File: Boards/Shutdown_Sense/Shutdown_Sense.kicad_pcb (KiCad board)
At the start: 2 copper layers, 76.2 x 67.3 mm, 68 parts, among them IC1 ATMEGA16M1, J2 MM_F_RA_20, J3 CONN_02X03, Q3 SSM3K333R, Q4 SSM3K333R, U101 TPS560430YF, U3 CAN_Transceiver, Y1 Crystal_SMD

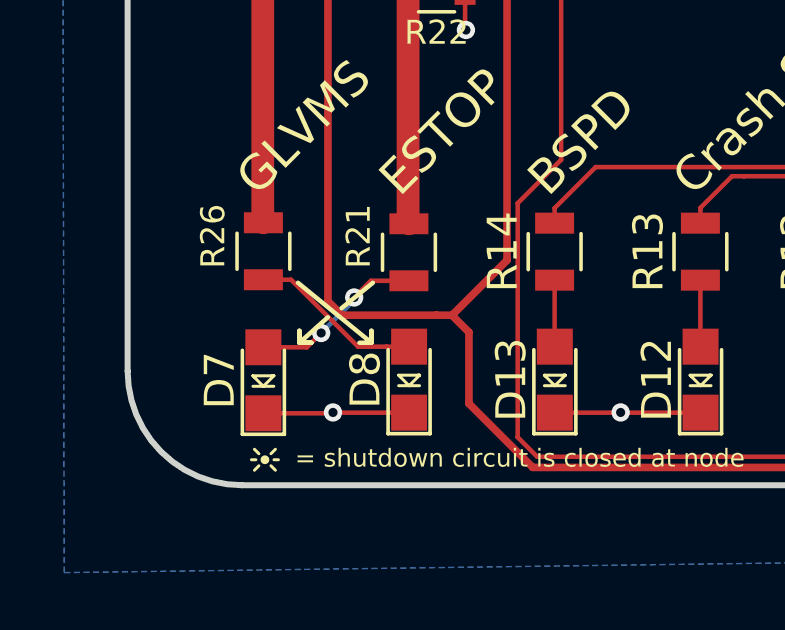
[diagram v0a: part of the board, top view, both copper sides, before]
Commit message: Fix SR-latch language in BSPD schematic
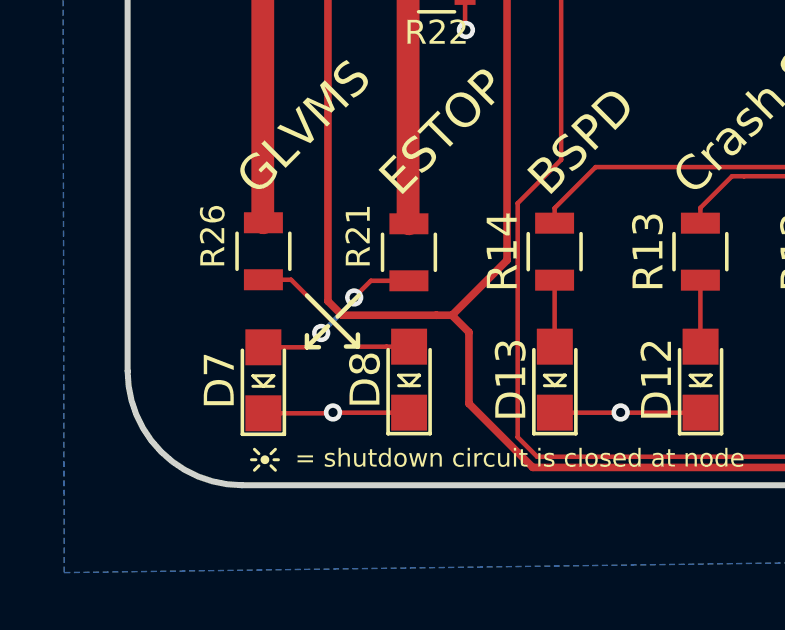
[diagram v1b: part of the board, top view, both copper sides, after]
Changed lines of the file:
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@@
   (general
     (thickness 1.6)
-    (drawings 92)
+    (drawings 89)
     (tracks 541)
     (zones 0)
@@
     (34 B.Paste user)
     (35 F.Paste user)
-    (36 B.SilkS user)
+    (36 B.SilkS user hide)
     (37 F.SilkS user)
     (38 B.Mask user)
@@
   )
   (setup
-    (last_trace_width 0.762)
+    (last_trace_width 0.1524)
     (user_trace_width 0.254)
     (user_trace_width 0.381)
@@
   (gr_line (start 203.2 100.7) (end 203.35 100.7) (layer F.SilkS) (width 0.1))
   (gr_circle (center 202.9 100.7) (end 202.95 100.75) (layer F.SilkS) (width 0.15))
-  (gr_line (start 204.05 96.4) (end 204.05 96.8) (layer F.SilkS) (width 0.15))
-  (gr_line (start 204.05 96.8) (end 204.05 96.4) (layer F.SilkS) (width 0.15))
-  (gr_line (start 204.45 96.8) (end 204.05 96.8) (layer F.SilkS) (width 0.15))
-  (gr_line (start 204.05 96.8) (end 204.45 96.8) (layer F.SilkS) (width 0.15))
-  (gr_line (start 206.45 96.8) (end 206.05 96.8) (layer F.SilkS) (width 0.15))
-  (gr_line (start 206.45 96.4) (end 206.45 96.8) (layer F.SilkS) (width 0.15))
-  (gr_line (start 206.45 96.8) (end 206.45 96.4) (layer F.SilkS) (width 0.15))
-  (gr_line (start 205 95.95) (end 204.05 96.8) (layer F.SilkS) (width 0.15))
-  (gr_line (start 206.5 94.8) (end 205.45 95.65) (layer F.SilkS) (width 0.15))
-  (gr_line (start 204 94.8) (end 206.45 96.8) (layer F.SilkS) (width 0.15))
+  (gr_line (start 204.3 96.55) (end 204.3 96.95) (layer F.SilkS) (width 0.15))
+  (gr_line (start 204.7 96.95) (end 204.3 96.95) (layer F.SilkS) (width 0.15))
+  (gr_line (start 206 96.925) (end 205.6 96.925) (layer F.SilkS) (width 0.15))
+  (gr_line (start 206 96.925) (end 206 96.525) (layer F.SilkS) (width 0.15))
+  (gr_line (start 205 96.25) (end 204.3 96.95) (layer F.SilkS) (width 0.15))
+  (gr_line (start 206.025 95.225) (end 205.325 95.925) (layer F.SilkS) (width 0.15))
+  (gr_line (start 204.3 95.225) (end 206 96.925) (layer F.SilkS) (width 0.15))
   (gr_text "Placement of SS_ESTOP and SS_GLVMS circuits\nare flipped until the junction of the resistor and\nthe LED. This was because of sizing issues with\nthe micromatch and CAN lines.\n\nThe shutdown circuit node labels correspond to the LEDs." (at 201 50.75) (layer B.SilkS)
     (effects (font (size 1 1) (thickness 0.125)) (justify right mirror))
